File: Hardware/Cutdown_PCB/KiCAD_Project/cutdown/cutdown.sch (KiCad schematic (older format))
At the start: 64 parts, among them J1 Mini_USB_B, J3 External Cutdown, J4 ISP, Q1 2N7002, SW1 SW_SPST, U1 FT231XS, U2 SPX3819M5-L-3-3, U3 ATmega328P-AU, U5 XBee, Y1 8MHz

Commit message: Reannotate
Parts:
- gave numbers to parts that had none: 2
- renumbered C14 to C13, C15 to C14, C16 to C15, C17 to C16, J3 to J2, J4 to J3, R16 to R15, R17 to R16, R18 to R17, R19 to R18, R20 to R19, R21 to R20, R22 to R21, R23 to R22, R24 to R23, U5 to U4

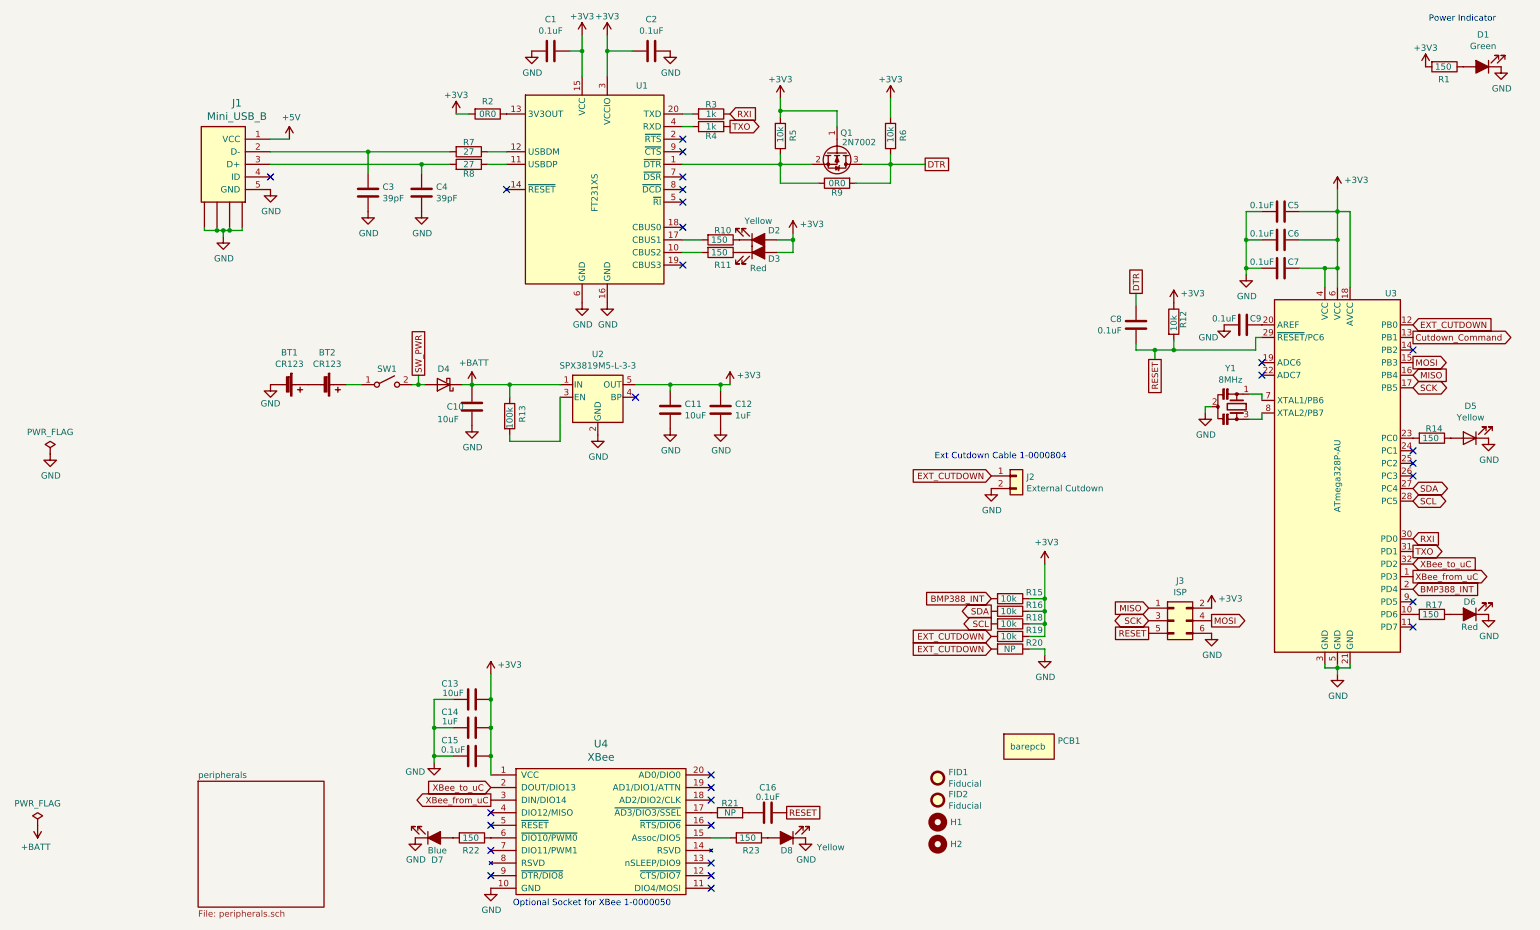
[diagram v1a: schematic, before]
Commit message: Add Arm LED and improve board layout
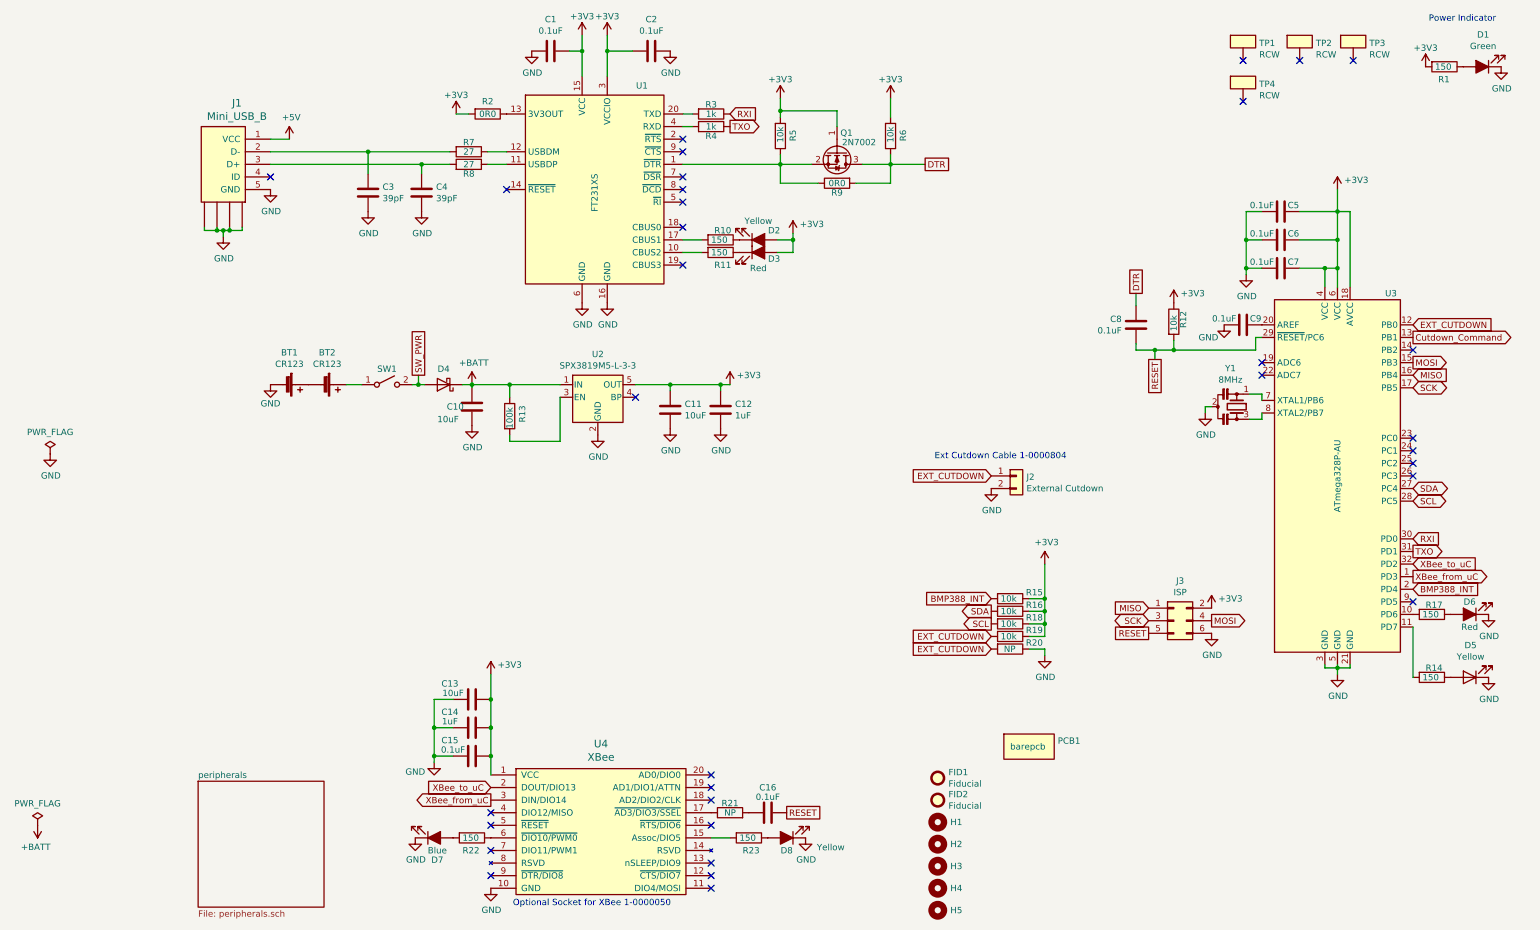
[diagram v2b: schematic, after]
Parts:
- added H3, H4, H5: M3_ISO_7380, mechanical:MountingHole_3.2mm_M3_ISO7380, symbol mechanical:M3_ISO_7380
- added TP1, TP2, TP3, TP4: 1-0000952, test_points:1-0000952, symbol test_points:1-0000952
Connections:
- net at U3.11 (PD7): now also R14.2
- net at U3.23 (PC0): no longer R14.2
- no-connect marks 29 -> 33
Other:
- moved on the sheet: D5, R14
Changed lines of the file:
@@
 $EndComp
 NoConn ~ 10225 5225
-NoConn ~ 10225 5425
 NoConn ~ 10225 4225
 NoConn ~ 10225 4125
@@
 L resistors_0603:1-0000008 R14
 U 1 1 618DC6D0
-P 10375 3925
-F 0 "R14" V 10300 3875 50  0000 L CNN
-F 1 "1-0000008" V 10375 3925 50  0001 C CNN
-F 2 "resistors_0603:1-0000008" V 10305 3925 50  0001 C CNN
-F 3 "~" H 10375 3925 50  0001 C CNN
-F 4 "1-0000008" H 10375 3925 50  0001 C CNN "Internal Part Number"
-F 5 "1" H 10375 3925 50  0001 C CNN "Populated"
-F 6 "150" V 10375 3850 50  0000 L CNN "PValue"
-	1    10375 3925
+P 10375 5825
+F 0 "R14" V 10300 5775 50  0000 L CNN
+F 1 "1-0000008" V 10375 5825 50  0001 C CNN
+F 2 "resistors_0603:1-0000008" V 10305 5825 50  0001 C CNN
+F 3 "~" H 10375 5825 50  0001 C CNN
+F 4 "1-0000008" H 10375 5825 50  0001 C CNN "Internal Part Number"
+F 5 "1" H 10375 5825 50  0001 C CNN "Populated"
+F 6 "150" V 10375 5750 50  0000 L CNN "PValue"
+	1    10375 5825
 	0    1    1    0
 $EndComp
@@
 L leds_0805:1-0000601 D5
 U 1 1 618DDD37
-P 10675 3925
-F 0 "D5" H 10668 3670 50  0000 C CNN
-F 1 "1-0000601" H 10675 3825 50  0001 C CNN
-F 2 "leds_0805:1-0000601" H 10675 3925 50  0001 C CNN
-F 3 "~" H 10675 3925 50  0001 C CNN
-F 4 "1-0000601" H 10675 3925 50  0001 C CNN "Internal Part Number"
-F 5 "1" H 10675 3925 50  0001 C CNN "Populated"
-F 6 "Yellow" H 10668 3761 50  0000 C CNN "PValue"
-	1    10675 3925
+P 10675 5825
+F 0 "D5" H 10668 5570 50  0000 C CNN
+F 1 "1-0000601" H 10675 5725 50  0001 C CNN
+F 2 "leds_0805:1-0000601" H 10675 5825 50  0001 C CNN
+F 3 "~" H 10675 5825 50  0001 C CNN
+F 4 "1-0000601" H 10675 5825 50  0001 C CNN "Internal Part Number"
+F 5 "1" H 10675 5825 50  0001 C CNN "Populated"
+F 6 "Yellow" H 10668 5661 50  0000 C CNN "PValue"
+	1    10675 5825
 	-1   0    0    1
 $EndComp
@@
 L power:GND #PWR030
 U 1 1 618DEED9
-P 10825 3925
-F 0 "#PWR030" H 10825 3675 50  0001 C CNN
-F 1 "GND" H 10830 3752 50  0000 C CNN
-F 2 "" H 10825 3925 50  0001 C CNN
-F 3 "" H 10825 3925 50  0001 C CNN
-	1    10825 3925
-	1    0    0    -1
-$EndComp
+P 10825 5825
+F 0 "#PWR030" H 10825 5575 50  0001 C CNN
+F 1 "GND" H 10830 5652 50  0000 C CNN
+F 2 "" H 10825 5825 50  0001 C CNN
+F 3 "" H 10825 5825 50  0001 C CNN
+	1    10825 5825
+	1    0    0    -1
+$EndComp
+$Comp
+L test_points:1-0000952 TP1
+U 1 1 6184BEAE
+P 8875 775
+F 0 "TP1" H 9003 763 50  0000 L CNN
+F 1 "1-0000952" H 8725 825 50  0001 C CNN
+F 2 "test_points:1-0000952" H 8925 725 50  0001 C CNN
+F 3 "~" H 8925 725 50  0001 C CNN
+F 4 "1-0000952" H 8725 725 50  0001 C CNN "Internal Part Number"
+F 5 "1" H 8875 925 50  0001 C CNN "Populated"
+F 6 "RCW" H 9003 672 50  0000 L CNN "PValue"
+	1    8875 775
+	1    0    0    -1
+$EndComp
+$Comp
+L test_points:1-0000952 TP2
+U 1 1 6184CDAF
+P 9325 775
+F 0 "TP2" H 9453 763 50  0000 L CNN
+F 1 "1-0000952" H 9175 825 50  0001 C CNN
+F 2 "test_points:1-0000952" H 9375 725 50  0001 C CNN
+F 3 "~" H 9375 725 50  0001 C CNN
+F 4 "1-0000952" H 9175 725 50  0001 C CNN "Internal Part Number"
+F 5 "1" H 9325 925 50  0001 C CNN "Populated"
+F 6 "RCW" H 9453 672 50  0000 L CNN "PValue"
+	1    9325 775
+	1    0    0    -1
+$EndComp
+$Comp
+L test_points:1-0000952 TP3
+U 1 1 6184D198
+P 9750 775
+F 0 "TP3" H 9878 763 50  0000 L CNN
+F 1 "1-0000952" H 9600 825 50  0001 C CNN
+F 2 "test_points:1-0000952" H 9800 725 50  0001 C CNN
+F 3 "~" H 9800 725 50  0001 C CNN
+F 4 "1-0000952" H 9600 725 50  0001 C CNN "Internal Part Number"
+F 5 "1" H 9750 925 50  0001 C CNN "Populated"
+F 6 "RCW" H 9878 672 50  0000 L CNN "PValue"
+	1    9750 775
+	1    0    0    -1
+$EndComp
+NoConn ~ 9750 925
+NoConn ~ 9325 925
+NoConn ~ 8875 925
+$Comp
+L test_points:1-0000952 TP4
+U 1 1 61865EBA
+P 8875 1100
+F 0 "TP4" H 9003 1088 50  0000 L CNN
+F 1 "1-0000952" H 8725 1150 50  0001 C CNN
+F 2 "test_points:1-0000952" H 8925 1050 50  0001 C CNN
+F 3 "~" H 8925 1050 50  0001 C CNN
+F 4 "1-0000952" H 8725 1050 50  0001 C CNN "Internal Part Number"
+F 5 "1" H 8875 1250 50  0001 C CNN "Populated"
+F 6 "RCW" H 9003 997 50  0000 L CNN "PValue"
+	1    8875 1100
+	1    0    0    -1
+$EndComp
+NoConn ~ 8875 1250
+Wire Wire Line
+	10225 5425 10225 5825
+NoConn ~ 10225 3925
+$Comp
+L mechanical:M3_ISO_7380 H3
+U 1 1 6185DBF3
+P 6450 7325
+F 0 "H3" H 6550 7325 50  0000 L CNN
+F 1 "M3_ISO_7380" H 6450 7450 50  0001 C CNN
+F 2 "mechanical:MountingHole_3.2mm_M3_ISO7380" H 6450 7325 50  0001 C CNN
+F 3 "None" H 6450 7325 50  0001 C CNN
+F 4 "0-0000000" H 6450 7325 50  0001 C CNN "Internal Part Number"
+F 5 "0" H 6450 7325 50  0001 C CNN "Populated"
+F 6 "M3" H 6450 7325 50  0001 C CNN "PValue"
+	1    6450 7325
+	1    0    0    -1
+$EndComp
+$Comp
+L mechanical:M3_ISO_7380 H4
+U 1 1 6185E088
+P 6450 7500
+F 0 "H4" H 6550 7500 50  0000 L CNN
+F 1 "M3_ISO_7380" H 6450 7625 50  0001 C CNN
+F 2 "mechanical:MountingHole_3.2mm_M3_ISO7380" H 6450 7500 50  0001 C CNN
+F 3 "None" H 6450 7500 50  0001 C CNN
+F 4 "0-0000000" H 6450 7500 50  0001 C CNN "Internal Part Number"
+F 5 "0" H 6450 7500 50  0001 C CNN "Populated"
+F 6 "M3" H 6450 7500 50  0001 C CNN "PValue"
+	1    6450 7500
+	1    0    0    -1
+$EndComp
+$Comp
+L mechanical:M3_ISO_7380 H5
+U 1 1 61879283
+P 6450 7675
+F 0 "H5" H 6550 7675 50  0000 L CNN
+F 1 "M3_ISO_7380" H 6450 7800 50  0001 C CNN
+F 2 "mechanical:MountingHole_3.2mm_M3_ISO7380" H 6450 7675 50  0001 C CNN
+F 3 "None" H 6450 7675 50  0001 C CNN
+F 4 "0-0000000" H 6450 7675 50  0001 C CNN "Internal Part Number"
+F 5 "0" H 6450 7675 50  0001 C CNN "Populated"
+F 6 "M3" H 6450 7675 50  0001 C CNN "PValue"
+	1    6450 7675
+	1    0    0    -1
+$EndComp

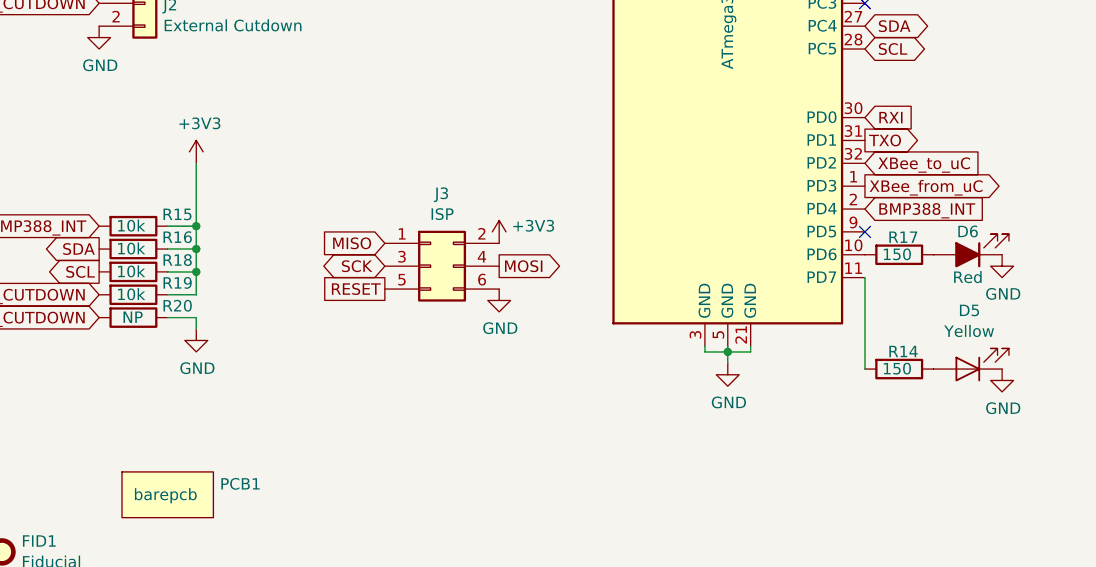
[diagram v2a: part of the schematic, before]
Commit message: Create Rev 3.1 production files
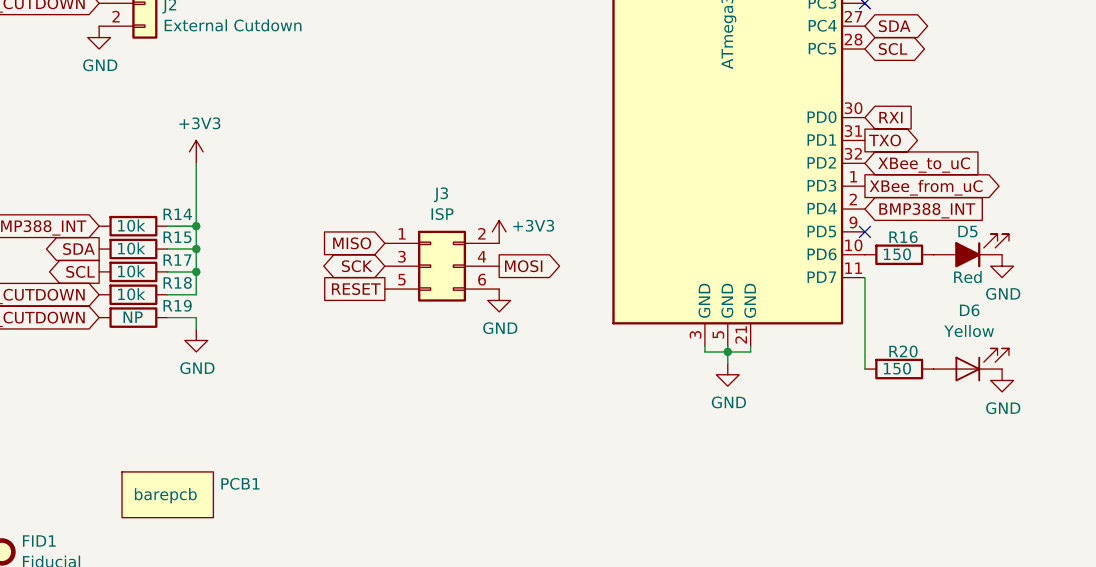
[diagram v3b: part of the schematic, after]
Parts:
- PCB1: Internal Part Number 3-0000070 -> 3-0000106
- renumbered D6 to D5, D5 to D6, R15 to R14, R16 to R15, R17 to R16, R18 to R17, R19 to R18, R20 to R19, R14 to R20
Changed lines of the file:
@@
 Sheet 1 2
 Title "Cutdown Module - NSSL EFM"
-Date "2020-12-22"
-Rev "3.0"
+Date "2021-11-09"
+Rev "3.1"
 Comp "Leeman Geophysical LLC"
 Comment1 "(479) 373-3736"
@@
 SDA
 $Comp
-L power:+3V3 #PWR033
+L power:+3V3 #PWR032
 U 1 1 5DE89C24
 P 7300 4925
-F 0 "#PWR033" H 7300 4775 50  0001 C CNN
+F 0 "#PWR032" H 7300 4775 50  0001 C CNN
 F 1 "+3V3" H 7315 5098 50  0000 C CNN
 F 2 "" H 7300 4925 50  0001 C CNN
@@
 $EndComp
 $Comp
-L Device:R R15
+L Device:R R14
 U 1 1 5DE8AF5D
 P 7025 5200
-F 0 "R15" V 6975 5325 50  0000 L CNN
+F 0 "R14" V 6975 5325 50  0000 L CNN
 F 1 "10k" V 7025 5125 50  0000 L CNN
 F 2 "Resistor_SMD:R_0603_1608Metric" V 6955 5200 50  0001 C CNN
@@
 $EndComp
 $Comp
-L Device:R R16
+L Device:R R15
 U 1 1 5DE8B206
 P 7025 5300
-F 0 "R16" V 6975 5425 50  0000 L CNN
+F 0 "R15" V 6975 5425 50  0000 L CNN
 F 1 "10k" V 7025 5225 50  0000 L CNN
 F 2 "Resistor_SMD:R_0603_1608Metric" V 6955 5300 50  0001 C CNN
@@
 $EndComp
 $Comp
-L Device:R R18
+L Device:R R17
 U 1 1 5DE8B4DA
 P 7025 5400
-F 0 "R18" V 6975 5525 50  0000 L CNN
+F 0 "R17" V 6975 5525 50  0000 L CNN
 F 1 "10k" V 7025 5325 50  0000 L CNN
 F 2 "Resistor_SMD:R_0603_1608Metric" V 6955 5400 50  0001 C CNN
@@
 EXT_CUTDOWN
 $Comp
-L Device:R R19
+L Device:R R18
 U 1 1 5DED1438
 P 7025 5500
-F 0 "R19" V 6975 5625 50  0000 L CNN
+F 0 "R18" V 6975 5625 50  0000 L CNN
 F 1 "10k" V 7025 5425 50  0000 L CNN
 F 2 "Resistor_SMD:R_0603_1608Metric" V 6955 5500 50  0001 C CNN
@@
 EXT_CUTDOWN
 $Comp
-L Device:R R20
+L Device:R R19
 U 1 1 5DED1B07
 P 7025 5600
-F 0 "R20" V 6975 5725 50  0000 L CNN
+F 0 "R19" V 6975 5725 50  0000 L CNN
 F 1 "NP" V 7025 5550 50  0000 L CNN
 F 2 "Resistor_SMD:R_0603_1608Metric" V 6955 5600 50  0001 C CNN
@@
 $EndComp
 $Comp
-L power:GND #PWR037
+L power:GND #PWR036
 U 1 1 5DED20EB
 P 7300 5650
-F 0 "#PWR037" H 7300 5400 50  0001 C CNN
+F 0 "#PWR036" H 7300 5400 50  0001 C CNN
 F 1 "GND" H 7305 5477 50  0000 C CNN
 F 2 "" H 7300 5650 50  0001 C CNN
@@
 NoConn ~ 9025 3325
 $Comp
-L power:GND #PWR039
+L power:GND #PWR038
 U 1 1 5FDC0D87
 P 9625 5800
-F 0 "#PWR039" H 9625 5550 50  0001 C CNN
+F 0 "#PWR038" H 9625 5550 50  0001 C CNN
 F 1 "GND" H 9630 5627 50  0000 C CNN
 F 2 "" H 9625 5800 50  0001 C CNN
@@
 $EndComp
 $Comp
-L Device:LED_ALT D6
+L Device:LED_ALT D5
 U 1 1 5FDEC312
 P 10675 5325
-F 0 "D6" H 10675 5225 50  0000 C CNN
+F 0 "D5" H 10675 5225 50  0000 C CNN
 F 1 "Red" H 10675 5425 50  0000 C CNN
 F 2 "LED_SMD:LED_0805_2012Metric" H 10675 5325 50  0001 C CNN
@@
 Connection ~ 2900 6000
 $Comp
-L power:+3V3 #PWR038
+L power:+3V3 #PWR037
 U 1 1 5FE05655
 P 2900 5800
-F 0 "#PWR038" H 2900 5650 50  0001 C CNN
+F 0 "#PWR037" H 2900 5650 50  0001 C CNN
 F 1 "+3V3" H 3050 5875 50  0000 C CNN
 F 2 "" H 2900 5800 50  0001 C CNN
@@
 MOSI
 $Comp
-L power:GND #PWR036
+L power:GND #PWR035
 U 1 1 5FE268FF
 P 8625 5475
-F 0 "#PWR036" H 8625 5225 50  0001 C CNN
+F 0 "#PWR035" H 8625 5225 50  0001 C CNN
 F 1 "GND" H 8630 5302 50  0000 C CNN
 F 2 "" H 8625 5475 50  0001 C CNN
@@
 $EndComp
 $Comp
-L power:+3V3 #PWR034
+L power:+3V3 #PWR033
 U 1 1 5FE26DC8
 P 8625 5275
-F 0 "#PWR034" H 8625 5125 50  0001 C CNN
+F 0 "#PWR033" H 8625 5125 50  0001 C CNN
 F 1 "+3V3" H 8775 5350 50  0000 C CNN
 F 2 "" H 8625 5275 50  0001 C CNN
@@
 $EndComp
 $Comp
-L resistors_0603:1-0000008 R17
+L resistors_0603:1-0000008 R16
 U 1 1 5FE318B5
 P 10375 5325
-F 0 "R17" V 10300 5275 50  0000 L CNN
+F 0 "R16" V 10300 5275 50  0000 L CNN
 F 1 "1-0000008" V 10375 5325 50  0001 C CNN
 F 2 "resistors_0603:1-0000008" V 10305 5325 50  0001 C CNN
@@
 $EndComp
 $Comp
-L power:GND #PWR035
+L power:GND #PWR034
 U 1 1 5FE3602F
 P 10825 5325
-F 0 "#PWR035" H 10825 5075 50  0001 C CNN
+F 0 "#PWR034" H 10825 5075 50  0001 C CNN
 F 1 "GND" H 10830 5152 50  0000 C CNN
 F 2 "" H 10825 5325 50  0001 C CNN
@@
 F 2 "lib_fp:barepcb" H 7175 6375 50  0001 C CNN
 F 3 "" H 7175 6375 50  0001 C CNN
-F 4 "3-0000070" H 7175 6375 50  0001 C CNN "Internal Part Number"
+F 4 "3-0000106" H 7175 6375 50  0001 C CNN "Internal Part Number"
 F 5 "1" H 7175 6375 50  0001 C CNN "Populated"
 	1    7175 6375
@@
 $EndComp
 $Comp
-L power:GND #PWR032
+L power:GND #PWR031
 U 1 1 5FE544E3
 P 6875 4325
-F 0 "#PWR032" H 6875 4075 50  0001 C CNN
+F 0 "#PWR031" H 6875 4075 50  0001 C CNN
 F 1 "GND" H 6880 4152 50  0000 C CNN
 F 2 "" H 6875 4325 50  0001 C CNN
@@
 $EndComp
 $Comp
-L power:GND #PWR031
+L power:GND #PWR030
 U 1 1 5FE42E20
 P -600 4050
-F 0 "#PWR031" H -600 3800 50  0001 C CNN
+F 0 "#PWR030" H -600 3800 50  0001 C CNN
 F 1 "GND" H -595 3877 50  0000 C CNN
 F 2 "" H -600 4050 50  0001 C CNN
@@
 Connection ~ 2325 3500
 $Comp
-L resistors_0603:1-0000008 R14
+L resistors_0603:1-0000008 R20
 U 1 1 618DC6D0
 P 10375 5825
-F 0 "R14" V 10300 5775 50  0000 L CNN
+F 0 "R20" V 10300 5775 50  0000 L CNN
 F 1 "1-0000008" V 10375 5825 50  0001 C CNN
 F 2 "resistors_0603:1-0000008" V 10305 5825 50  0001 C CNN
@@
 $EndComp
 $Comp
-L leds_0805:1-0000601 D5
+L leds_0805:1-0000601 D6
 U 1 1 618DDD37
 P 10675 5825
-F 0 "D5" H 10668 5570 50  0000 C CNN
+F 0 "D6" H 10668 5570 50  0000 C CNN
 F 1 "1-0000601" H 10675 5725 50  0001 C CNN
 F 2 "leds_0805:1-0000601" H 10675 5825 50  0001 C CNN
@@
 $EndComp
 $Comp
-L power:GND #PWR030
+L power:GND #PWR039
 U 1 1 618DEED9
 P 10825 5825
-F 0 "#PWR030" H 10825 5575 50  0001 C CNN
+F 0 "#PWR039" H 10825 5575 50  0001 C CNN
 F 1 "GND" H 10830 5652 50  0000 C CNN
 F 2 "" H 10825 5825 50  0001 C CNN

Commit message: Make R9 no populate. Closes #57
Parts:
- R9: Populated 1 -> 0
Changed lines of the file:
@@
 F 3 "~" H 5650 1900 50  0001 C CNN
 F 4 "1-0000006" H 5650 1900 50  0001 C CNN "Internal Part Number"
-F 5 "1" H 5650 1900 50  0001 C CNN "Populated"
+F 5 "0" H 5650 1900 50  0001 C CNN "Populated"
 F 6 "0R0" V 5650 1900 50  0000 C CNN "PValue"
 	1    5650 1900
